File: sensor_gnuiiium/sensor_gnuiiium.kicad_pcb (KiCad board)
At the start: 2 copper layers, 75 x 40 mm, 37 parts, among them J1 jumper, J10 Conn_01x10_Male, J2 jumper, J3 jumper, J4 jumper, J5 jumper, J6 jumper, J7 jumper, J8 jumper, U1 qrd111x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

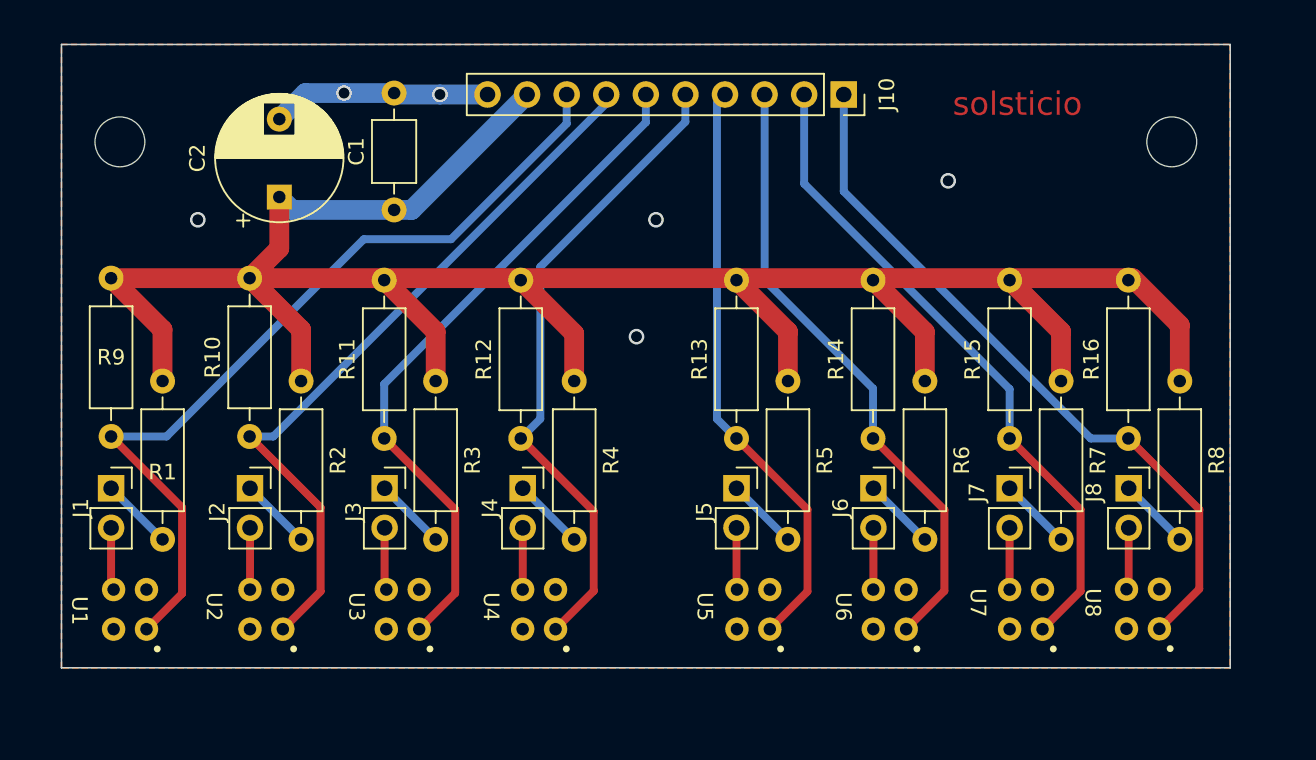
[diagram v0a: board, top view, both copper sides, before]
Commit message: changed to smd version
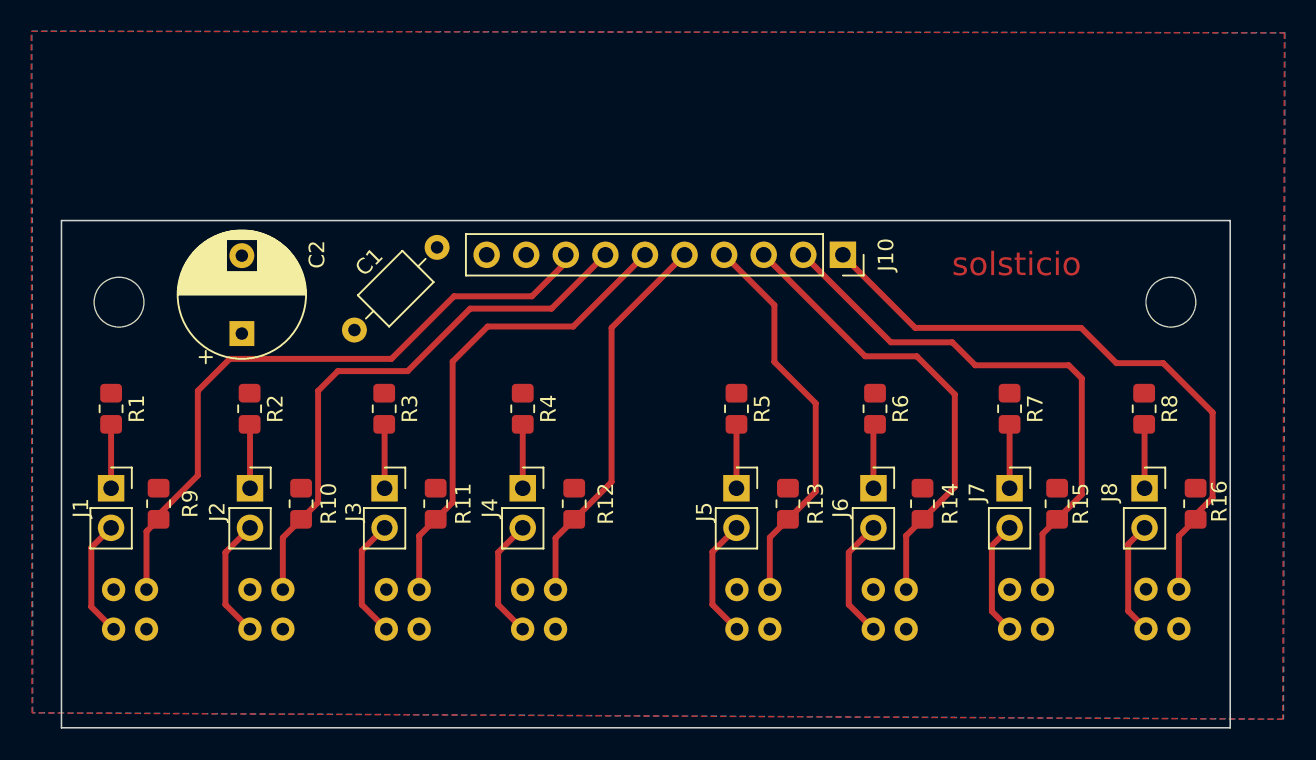
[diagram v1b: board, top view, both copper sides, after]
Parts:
- R1, R10, R11, R12, R13, R14, R15, R16, R2, R3, R4, R5, R6, R7, R8, R9: footprint Resistor_THT:R_Axial_DIN0207_L6.3mm_D2.5mm_P10.16mm_Horizontal -> Resistor_SMD:R_0805_2012Metric_Pad1.20x1.40mm_HandSolder
- U1, U2, U3, U4, U5, U6, U7, U8: moved to B.Cu
- moved REF** 10.3 mm to (145.5, 96.5)
- moved REF** 10.3 mm to (213.0, 96.5)
- moved J10 10.3 mm to (192.0, 93.5)
- moved C2 9.09 mm to (153.4, 98.6)
- moved C1 8.12 mm to (160.7, 98.3), turned to 45 degrees
- moved R16 6.02 mm to (214.6, 109.5)
- moved R10 5.44 mm to (157.2, 109.5)
- moved R12 5.42 mm to (174.8, 109.5)
- moved R11 5.34 mm to (165.9, 109.5)
- moved R13 5.34 mm to (188.5, 109.5)
- moved R9 5.29 mm to (148.1, 109.5)
- moved R14 5.26 mm to (197.1, 109.5)
- moved R15 5.18 mm to (205.7, 109.5)
- moved R1 3.75 mm to (145.0, 103.4)
- moved R4 3.75 mm to (171.4, 103.4)
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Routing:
- net +3V3: track 154.1 -> 0.00 mm
- net s3: track 41.6 -> 24.9 mm
- net GND: track 14.1 -> 0.00 mm, vias 6 -> 0
- net s2: track 44.1 -> 30.7 mm
- net s0: track 54.6 -> 41.6 mm
- net s4: track 37.9 -> 25.1 mm
- net s1: track 47.6 -> 35.7 mm
- net s5: track 40.1 -> 29.8 mm
- net s6: track 42.7 -> 35.8 mm
- net s7: track 46.2 -> 40.2 mm
- net Net-(J4-Pad2): track 3.96 -> 7.81 mm
- net Net-(J6-Pad2): track 3.97 -> 7.81 mm
- net Net-(J2-Pad2): track 3.96 -> 7.81 mm
- net Net-(J5-Pad2): track 3.97 -> 7.79 mm
- net Net-(J3-Pad2): track 4.01 -> 7.76 mm
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- added copper zone on F.Cu, net +3V3
- removed copper zone on F.Cu, net GND
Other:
- board size 75 x 40 mm -> 75 x 32.5 mm
